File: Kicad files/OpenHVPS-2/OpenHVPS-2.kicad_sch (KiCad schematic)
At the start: 67 parts, among them J1 Conn_01x03_Male, J2 Conn_01x03_Male, Q1 FQT7N10, Q2 BC846, Q3 MMDT3906, U1 74HC14, U2 MAX4162, U3 CD14538BM, U4 MAX6008AEUR+T

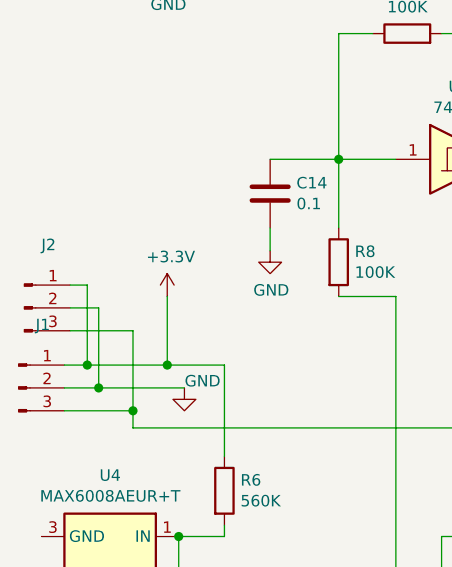
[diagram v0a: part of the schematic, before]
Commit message: Moved terminal bloack away from HV
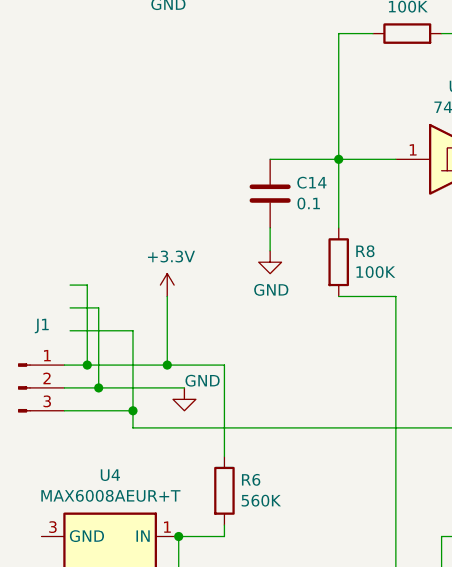
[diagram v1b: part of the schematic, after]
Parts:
- removed J2: Conn_01x03_Male, Connector_PinHeader_2.54mm:PinHeader_1x03_P2.54mm_Vertical, symbol Connector:Conn_01x03_Male
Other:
- title: OpenRover -> SafePulse
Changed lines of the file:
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@@
   (paper "A4")
   (title_block
-    (title "OpenRover")
-    (date "2021-01-10")
-    (rev "1")
+    (title "SafePulse")
+    (date "2021-01-15")
+    (rev "2.0")
     (company "SafeCast")
+    (comment 1 "Double Sided Version")
   )
   (junction (at 25.4 111.125) (diameter 1.016) (color 0 0 0 0))
@@
     )
   )
-  (symbol (lib_id "Connector:Conn_01x03_Male") (at 18.415 104.775 0) (unit 1)
-    (in_bom yes) (on_board yes)
-    (property "Reference" "J2" (id 0) (at 21.1074 97.7708 0))
-    (property "Value" "Conn_01x03_Male" (id 1) (at 21.107 100.07 0)
-      (effects (font (size 1.27 1.27)) hide)
-    )
-    (property "Footprint" "Connector_PinHeader_2.54mm:PinHeader_1x03_P2.54mm_Vertical" (id 2) (at 18.415 104.775 0)
-      (effects (font (size 1.27 1.27)) hide)
-    )
-    (property "Datasheet" "~" (id 3) (at 18.415 104.775 0)
-      (effects (font (size 1.27 1.27)) hide)
-    )
-  )
   (symbol (lib_id "Device:Ferrite_Bead") (at 81.28 28.575 0) (unit 1)
     (in_bom yes) (on_board yes)
@@
       (reference "J1") (unit 1) (value "Conn_01x03_Male") (footprint "Connector_PinHeader_2.54mm:PinHeader_1x03_P2.54mm_Vertical")
     )
-    (path "/64fe1763-fce1-4ab1-a949-fbdd5303c0a7"
-      (reference "J2") (unit 1) (value "Conn_01x03_Male") (footprint "Connector_PinHeader_2.54mm:PinHeader_1x03_P2.54mm_Vertical")
-    )
     (path "/00000000-0000-0000-0000-00005ffe44be"
